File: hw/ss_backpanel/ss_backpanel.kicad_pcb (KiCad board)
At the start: 2 copper layers, 165 x 51.1 mm, 0 parts

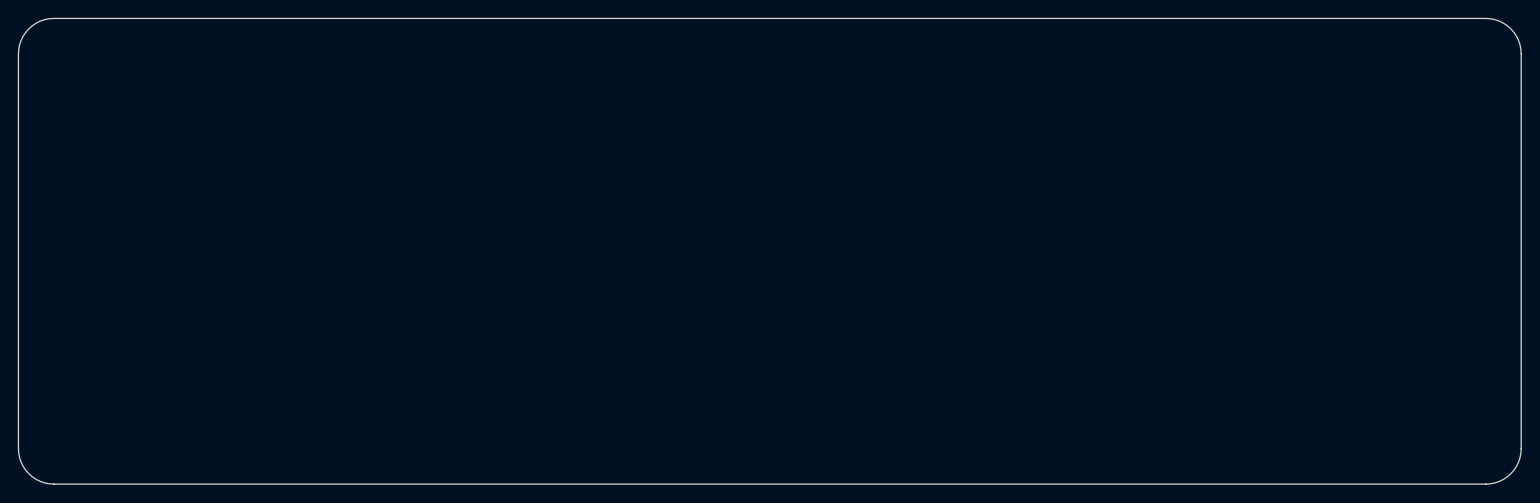
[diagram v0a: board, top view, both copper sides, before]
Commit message: Started on 1.6mm FR4 back-panel
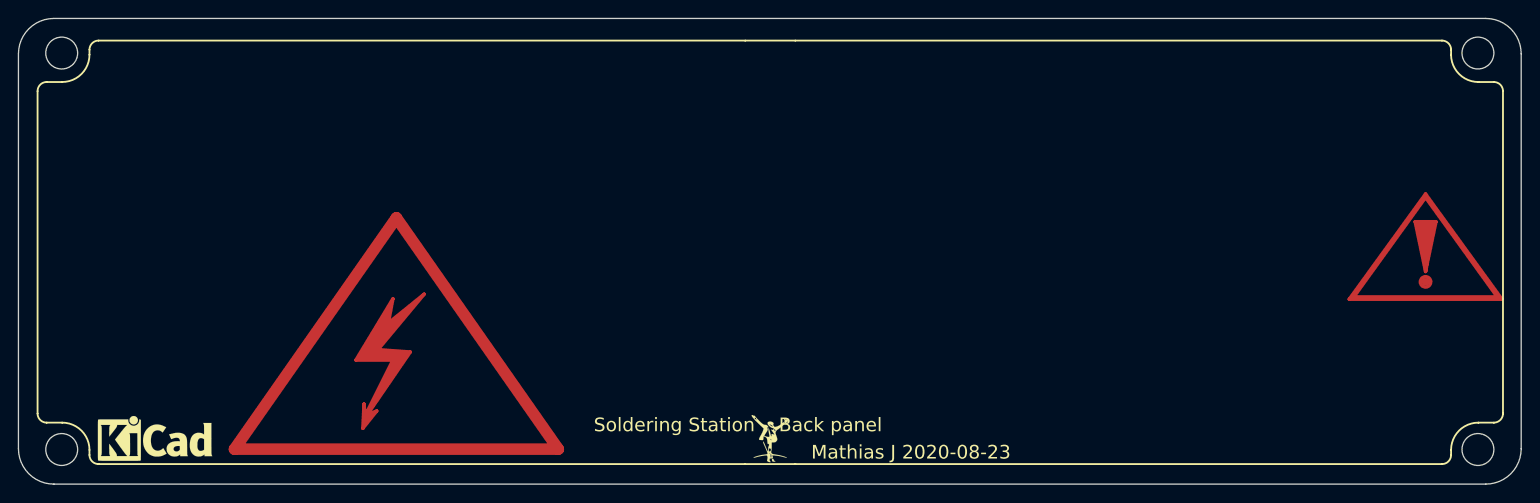
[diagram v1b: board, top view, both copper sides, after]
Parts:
- added H101: MountingHole, customlib_mj_fp:MountingHole_3.5mm_Hammond_panel_screws, F.Cu at (72.2, 52.7)
- added H102: MountingHole, customlib_mj_fp:MountingHole_3.5mm_Hammond_panel_screws, F.Cu at (227.8, 52.7)
- added H103: MountingHole, customlib_mj_fp:MountingHole_3.5mm_Hammond_panel_screws, F.Cu at (72.2, 96.2)
- added H104: MountingHole, customlib_mj_fp:MountingHole_3.5mm_Hammond_panel_screws, F.Cu at (227.8, 96.2)
- added LOGO101: Logo_Kicad_small, Symbol:KiCad-Logo_5mm_SilkScreen, F.Cu at (82.5, 95.5)
- added Logo101: Attention, Symbol:Symbol_Attention_CopperTop_Big, F.Cu at (222.0, 75.0)
- added Logo102: HighVoltage, Symbol:Symbol_HighVoltage_Type2_CopperTop_Big, F.Cu at (109.0, 86.0)
- added Logo103: MJ_Mini, customlib_mj_fp:MJ_Mini, F.Cu at (150.0, 95.0)
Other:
- board text added: "Mathias J 2020-08-23"
- board text added: "Soldering Station Back panel"

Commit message: Backpanel: Initial placement of Schaffner AC-inlet, Schurter secondary fuse-holder and 2x Weller DIN7
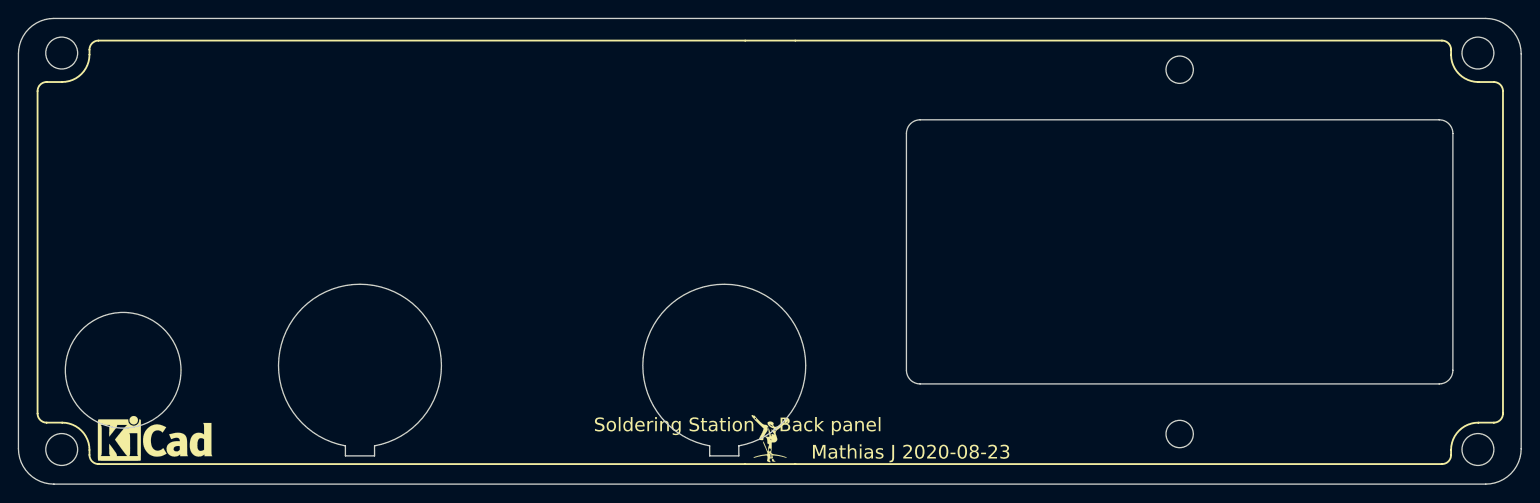
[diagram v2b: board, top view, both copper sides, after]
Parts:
- removed Logo101: Attention, Symbol:Symbol_Attention_CopperTop_Big
- removed Logo102: HighVoltage, Symbol:Symbol_HighVoltage_Type2_CopperTop_Big
- added M101: Amphenol_T3437000-DIN7_panel_cutout, customlib_mj_fp:Amphenol_T3437000-DIN7-panel_cutout, B.Cu at (105.0, 87.0)
- added M102: Amphenol_T3437000-DIN7_panel_cutout, customlib_mj_fp:Amphenol_T3437000-DIN7-panel_cutout, B.Cu at (145.0, 87.0)
- added M103: Schurter-3101_0060-fuse_holder-Panel_cutout, customlib_mj_fp:Schurter_3101_0060_fuse_holder-panel_cutout, F.Cu at (79.0, 87.5)
- added M104: FN283-1-06_Schaffner_AC-panel_cutout, customlib_mj_fp:FN283_panel_cutout-outside_mnt, B.Cu at (195.0, 74.5)

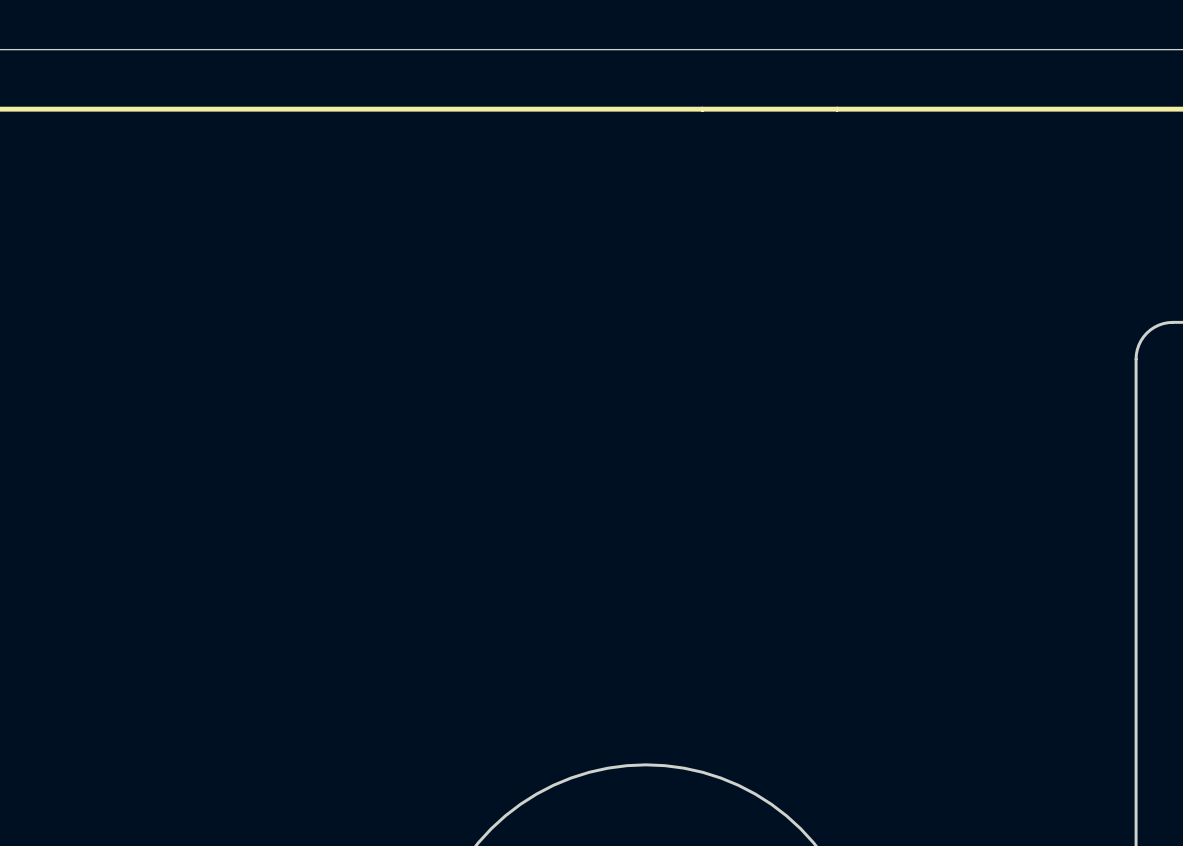
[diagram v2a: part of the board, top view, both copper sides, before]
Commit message: Added back-panel cutouts for Wurth RJ45 (LAN) and TE's USB-A & USB-B connectors
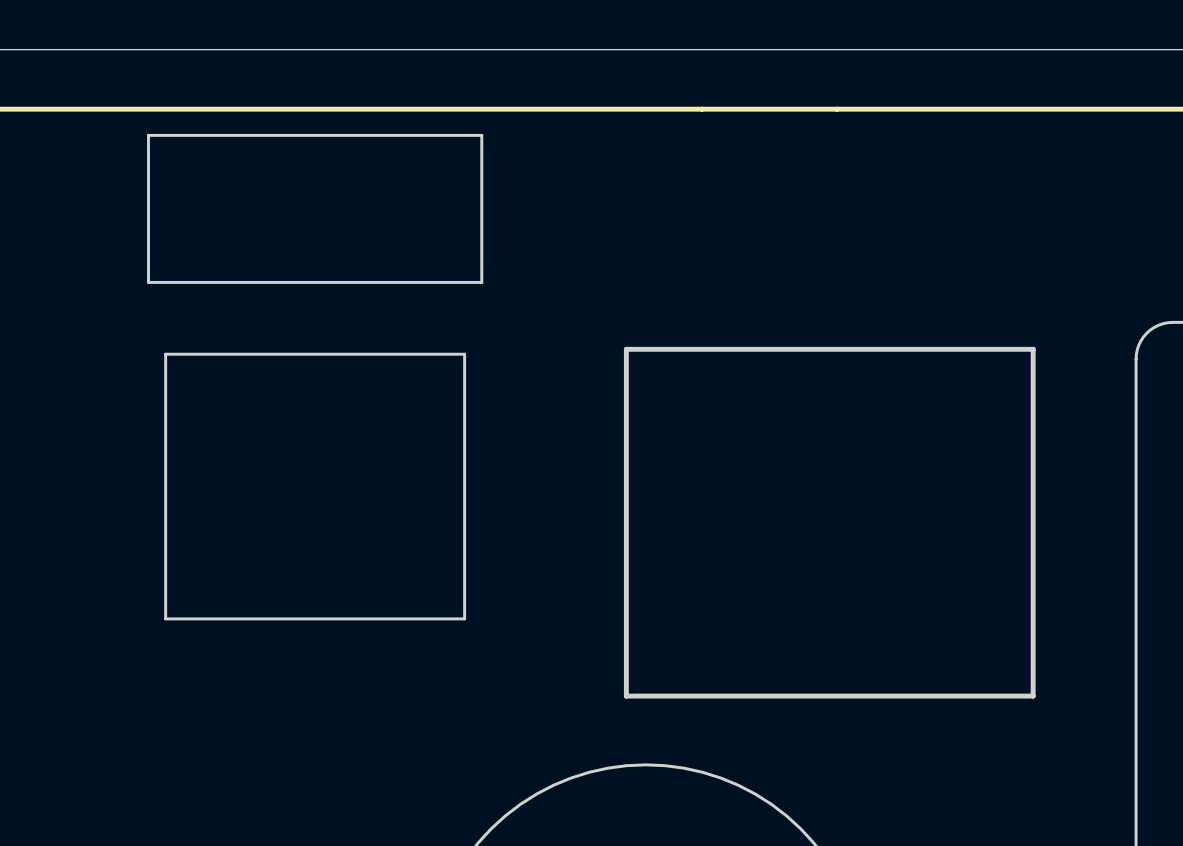
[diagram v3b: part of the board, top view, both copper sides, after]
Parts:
- added M105: 74980104400-Wurth_RJ45-Panel_cutout, customlib_mj_fp:74980104400_WE_RJ45_LAN-Panel_cutout, B.Cu at (152.5, 61.1)
- added M106: TE-1734346-Panel_cutout, customlib_mj_fp:TE_1734346-Panel_cutout, B.Cu at (131.5, 61.1)
- added M107: TE-1-292303-Panel_cutout, customlib_mj_fp:TE_1-292303-Panel_cutout, B.Cu at (131.5, 59.5)
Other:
- board text added: "(MB PCB - slot 2)"
- board text added: "PCB bottom: 100 - 38.9"

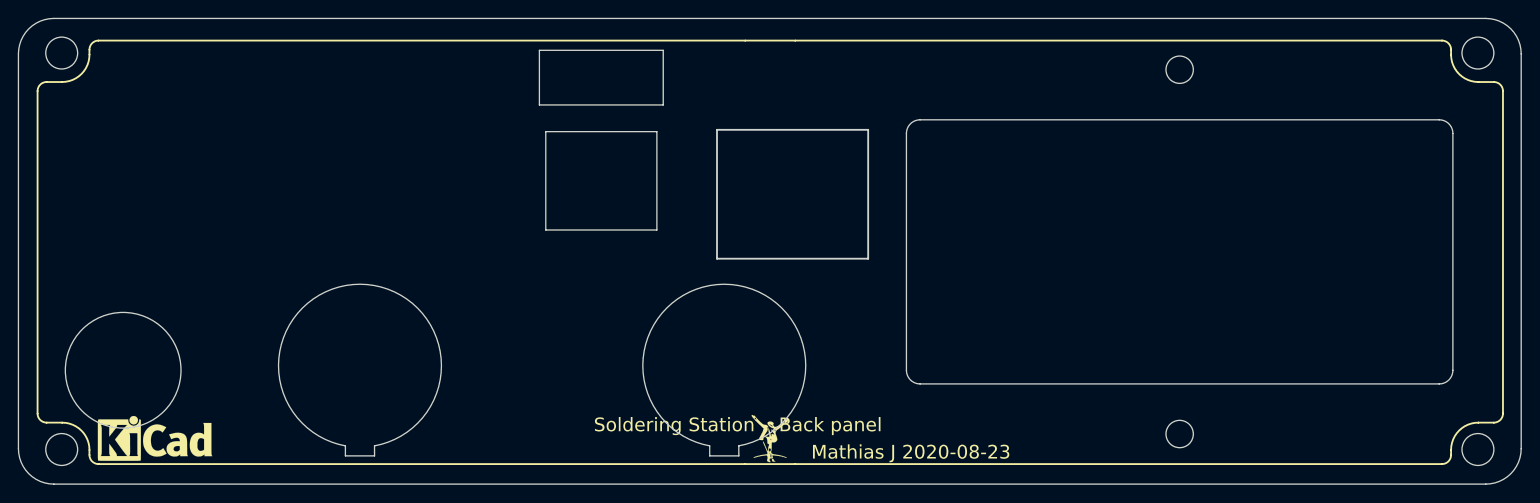
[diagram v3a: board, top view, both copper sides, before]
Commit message: Updated back-panel with 3.5mm audio jack & Dsub-9 cut-outs
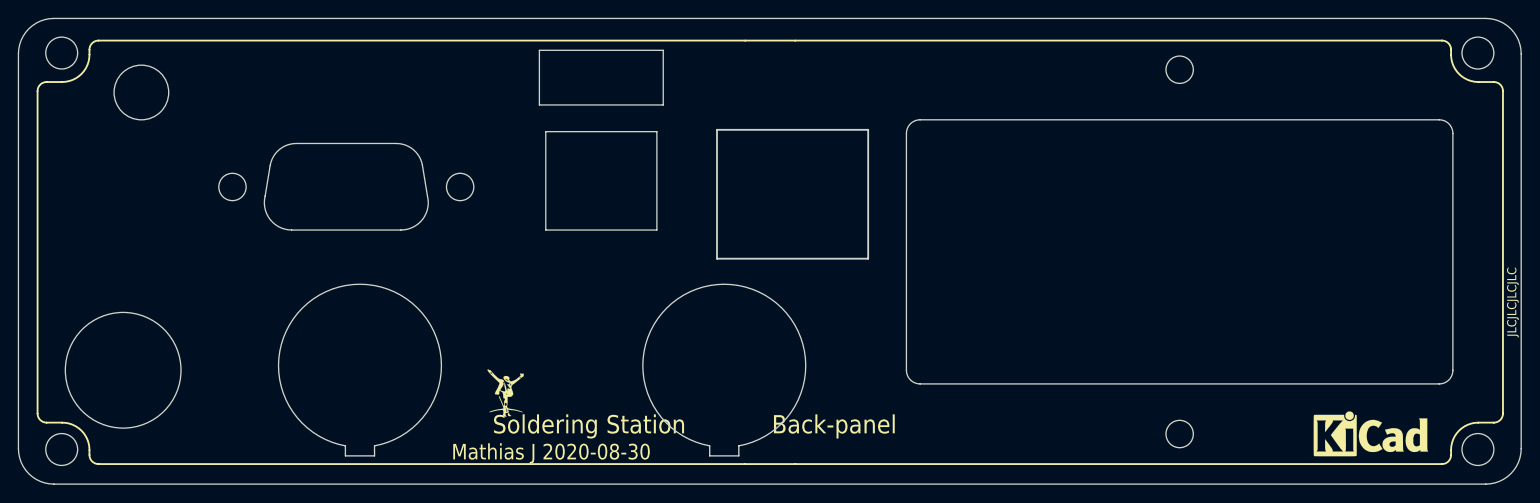
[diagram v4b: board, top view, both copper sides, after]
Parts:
- added M108: DSub9-Kycon_K22X-E9P-N-panel_cutout-small, customlib_mj_fp:DSub9-Kycon_K22X-E9P-N_panel_cutout_behind, B.Cu at (103.5, 61.1)
- added M109: SJ-3571N_CUI_audio_jacket_panel_cutout, customlib_mj_fp:SJ-3571N_panel_cutout, B.Cu at (81.0, 59.5)
- moved LOGO101 133.5 mm to (216.0, 95.0)
- moved Logo103 29.4 mm to (121.0, 90.0)
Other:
- board text added: "JLCJLCJLCJLC"
- board text added: "Mathias J 2020-08-30"
- board text added: "Soldering Station Back-panel"
- board text removed: "Mathias J 2020-08-23"
- board text removed: "Soldering Station Back panel"

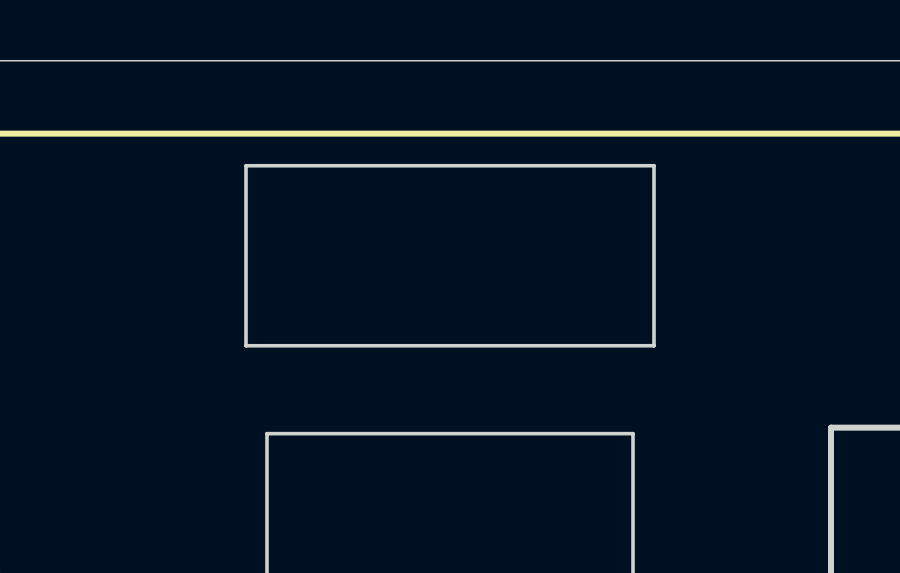
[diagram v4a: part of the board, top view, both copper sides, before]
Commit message: Updated USB-A conn to CUI UJ2-AH-1-SMT because retention pads are SMD. Also better USB-A cutout in back panel. Updated 3d test model
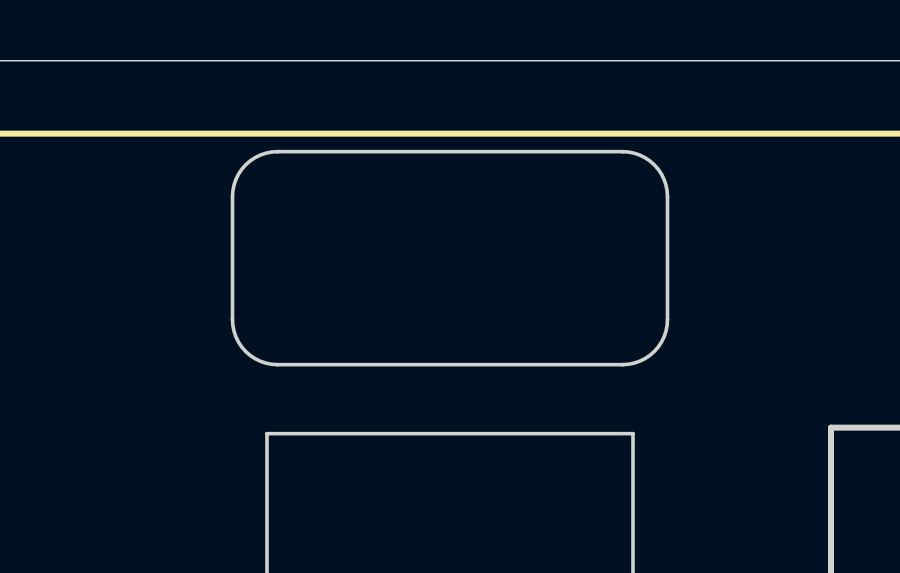
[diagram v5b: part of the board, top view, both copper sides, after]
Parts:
- M107: value TE-1-292303-Panel_cutout -> CUI-UJ2_AH_1_SMT-Panel_cutout; footprint customlib_mj_fp:TE_1-292303-Panel_cutout -> customlib_mj_fp:CUI-UJ2_AH_1_SMT-Panel_cutout

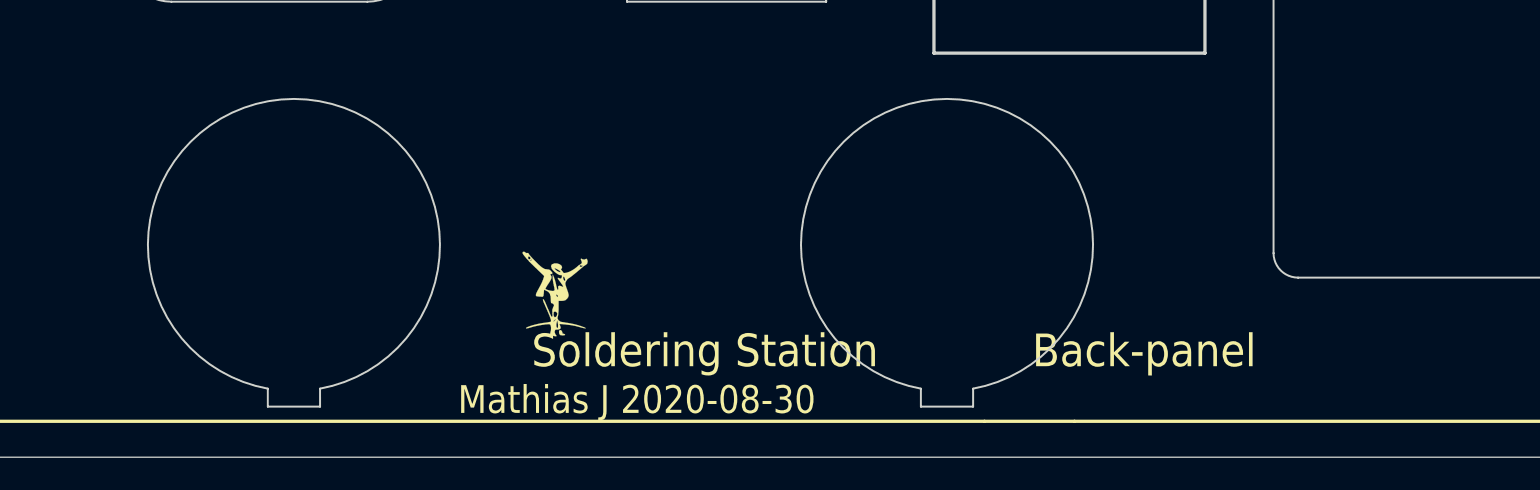
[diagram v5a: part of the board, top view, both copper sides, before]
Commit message: Added 4mm banana earth connector to back panel. Moved DIN-connectors slightly to fit. Updated 3d test model
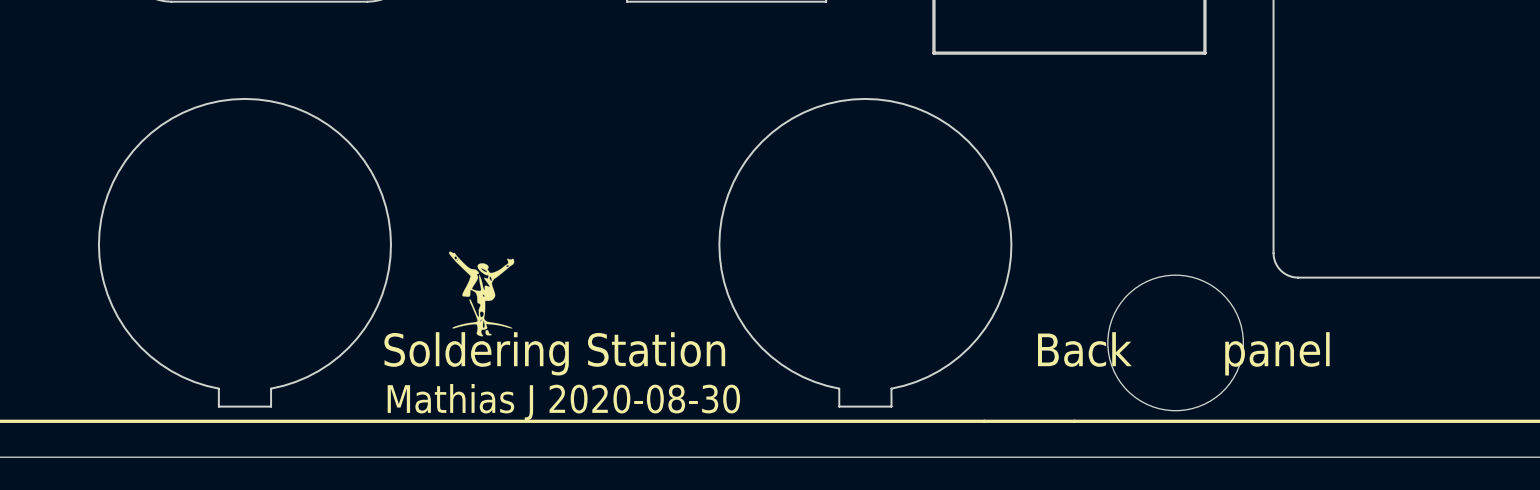
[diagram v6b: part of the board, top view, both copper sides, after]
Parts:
- added J101: 4mm_banana_socket-LB_I4R_A-panelmnt, customlib_mj_fp:LB_I4R_A-4mm_banana_socket_panelmnt, B.Cu at (159.0, 93.0)
- moved M102 5.00 mm to (140.0, 87.0)
- moved Logo103 4.50 mm to (116.5, 90.0)
- moved M101 3.00 mm to (102.0, 87.0)
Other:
- board text added: "Back panel"
- board text added: "Soldering Station"
- board text removed: "Soldering Station Back-panel"
